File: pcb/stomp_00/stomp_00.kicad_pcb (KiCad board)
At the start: 2 copper layers, 54 x 106 mm, 48 parts, among them J1 9V_Power_Input, J10 AudioJack3, J11 AudioJack3, J2 Conn_01x09, J3 GuitarInput1, J4 Headphones, J5 GuitarOutput1, J6 Conn_01x09, J7 Conn_02x04_Counter_Clockwise, SW1 SW_DIP_x04, SW2 Footswitch, U14 6N138, U2 TL072, U4 XL1509-5.0, U5 AP7333-33SRG, U7 Teensy4.1, U9 SGTL5000XNAA3

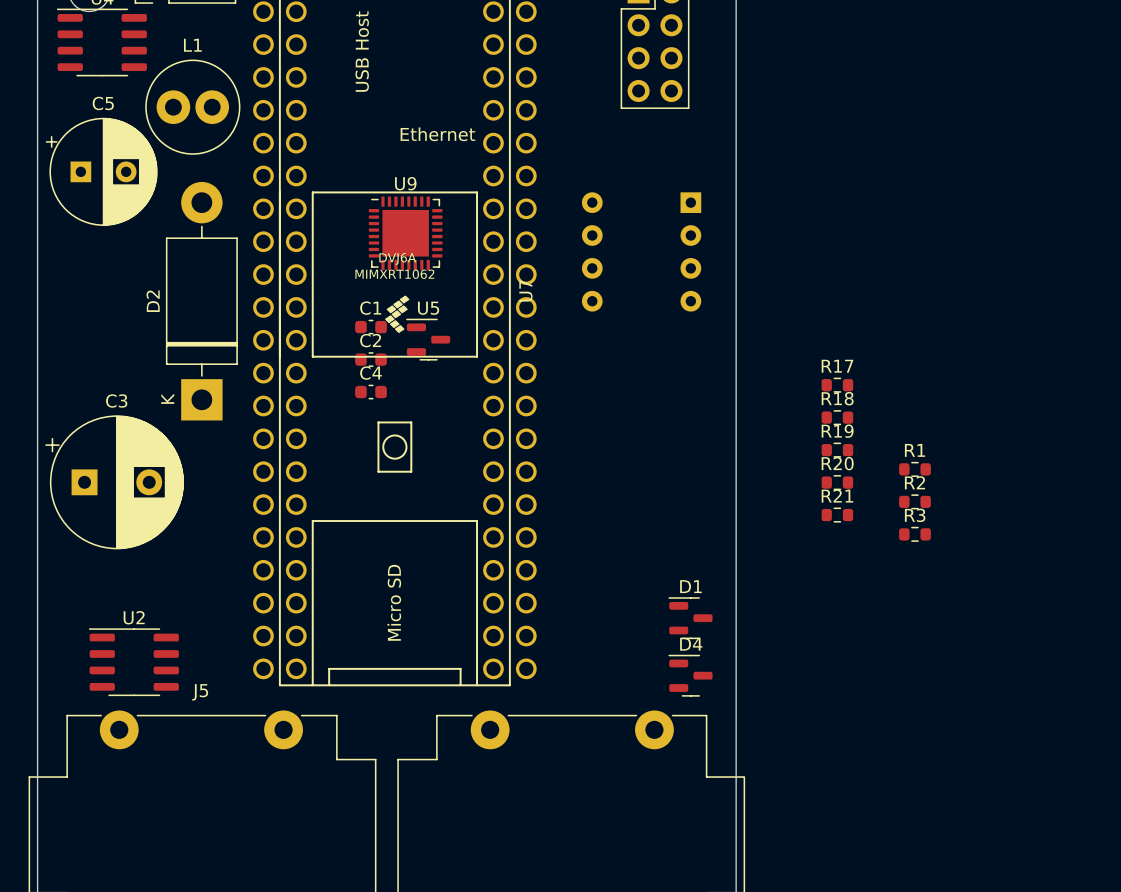
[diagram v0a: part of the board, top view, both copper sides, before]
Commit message: tweaking layout, issue with usb socket placement
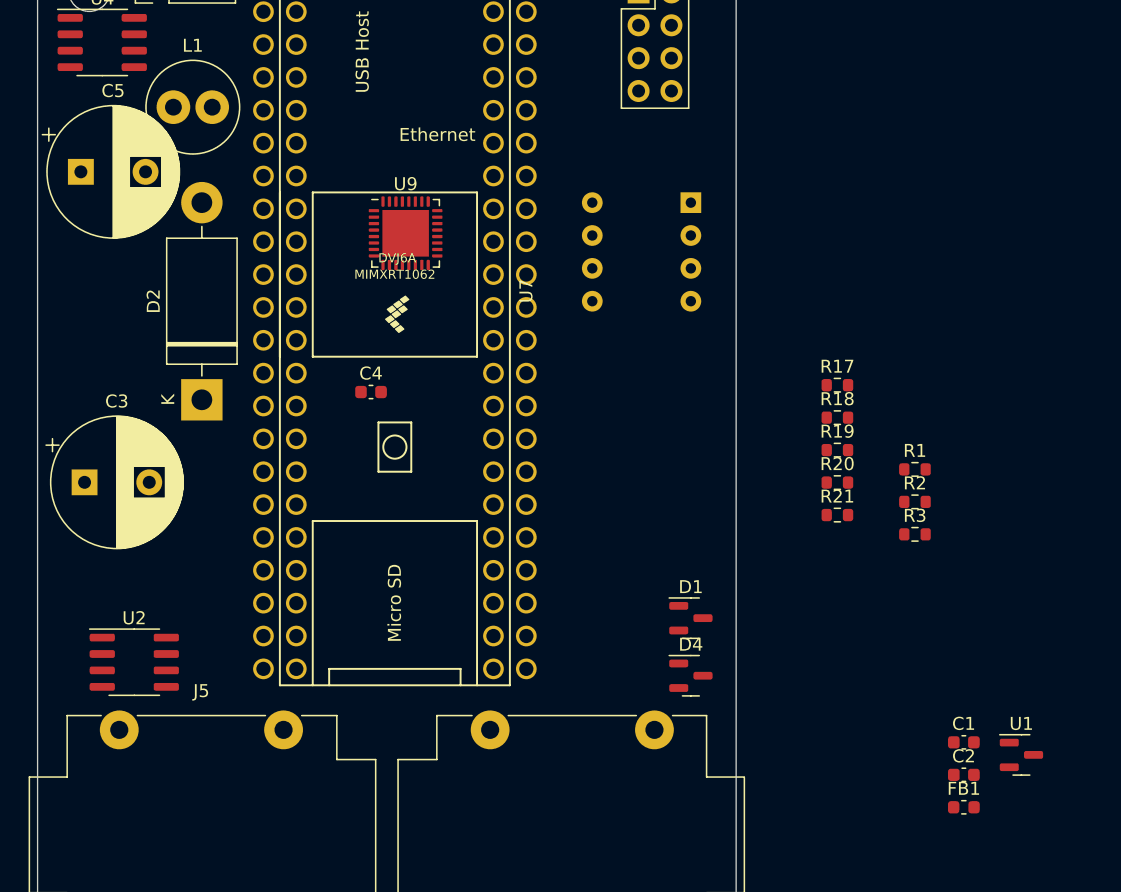
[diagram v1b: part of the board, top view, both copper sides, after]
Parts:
- removed U5: AP7333-33SRG, Package_TO_SOT_SMD:SOT-23
- added FB1: 600, Inductor_SMD:L_0603_1608Metric, F.Cu at (71.6, 71.1)
- added U1: AP7313-18SAG, Package_TO_SOT_SMD:SOT-23, F.Cu at (76.1, 67.1)
- C5: value 180uF 35V -> 470uF 25V; footprint Capacitor_THT:CP_Radial_D8.0mm_P3.50mm -> Capacitor_THT:CP_Radial_D10.0mm_P5.00mm
- J3, J5: footprint Connector_Audio:Jack_6.35mm_Neutrik_NMJ4HCD2_Horizontal -> stomp:Jack_6.35mm_Neutrik_NMJ4HCD2_Horizontal
- L1: value 68uH/2A -> 22uH/2A
- moved C2 56.0 mm to (71.6, 68.6)
- moved C1 56.0 mm to (71.6, 66.1)
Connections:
- net +3.3VDAC renamed +1V8
- C1 pad 1: +5V -> +3.3V
- U9 pad 5: +3.3V -> Net-(U9-VDDA)

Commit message: 9v power stuff
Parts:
- removed J1: 9V_Power_Input, Connector_PinHeader_2.54mm:PinHeader_1x03_P2.54mm_Vertical
- added J8: Barrel_Jack, Connector_PinHeader_2.54mm:PinHeader_1x02_P2.54mm_Vertical, F.Cu at (6.96, 2.00)
- moved C3 42.3 mm to (15.0, 5.25), turned to -90 degrees
- moved D2 39.0 mm to (23.5, 2.13), turned to -90 degrees
- moved SW1 37.8 mm to (23.6, 51.0)
- moved U2 28.0 mm to (35.5, 59.0)
- moved C4 26.4 mm to (16.5, 14.2)
- moved U9 18.8 mm to (40.5, 12.2)
- moved U4 12.9 mm to (16.5, 17.8)
- moved L1 12.6 mm to (20.8, 24.2)
- moved U7 10.0 mm to (37.6, 32.0)
- moved C5 7.40 mm to (9.87, 18.5), turned to 180 degrees

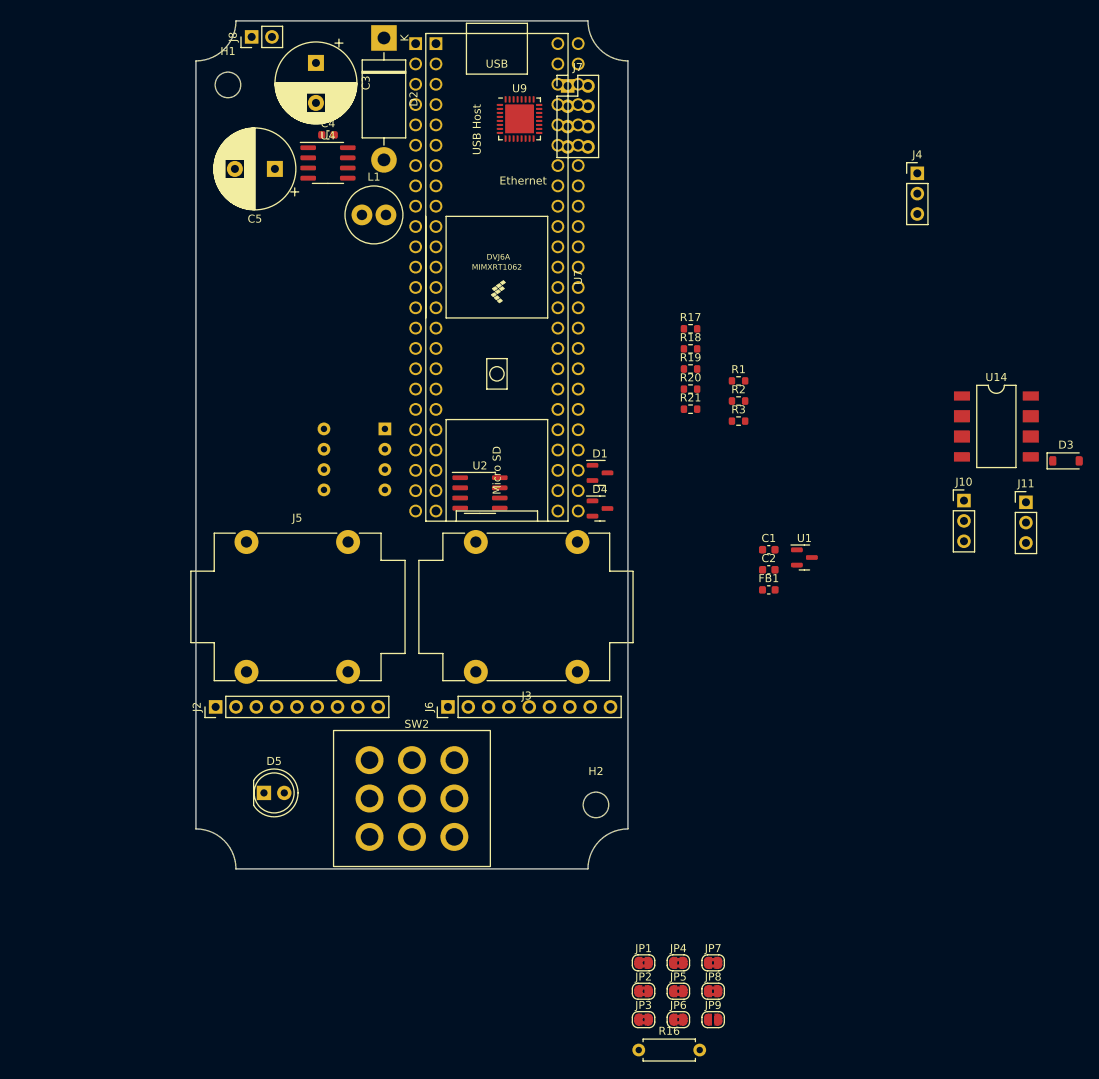
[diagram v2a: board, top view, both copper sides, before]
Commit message: changed voltage regulator
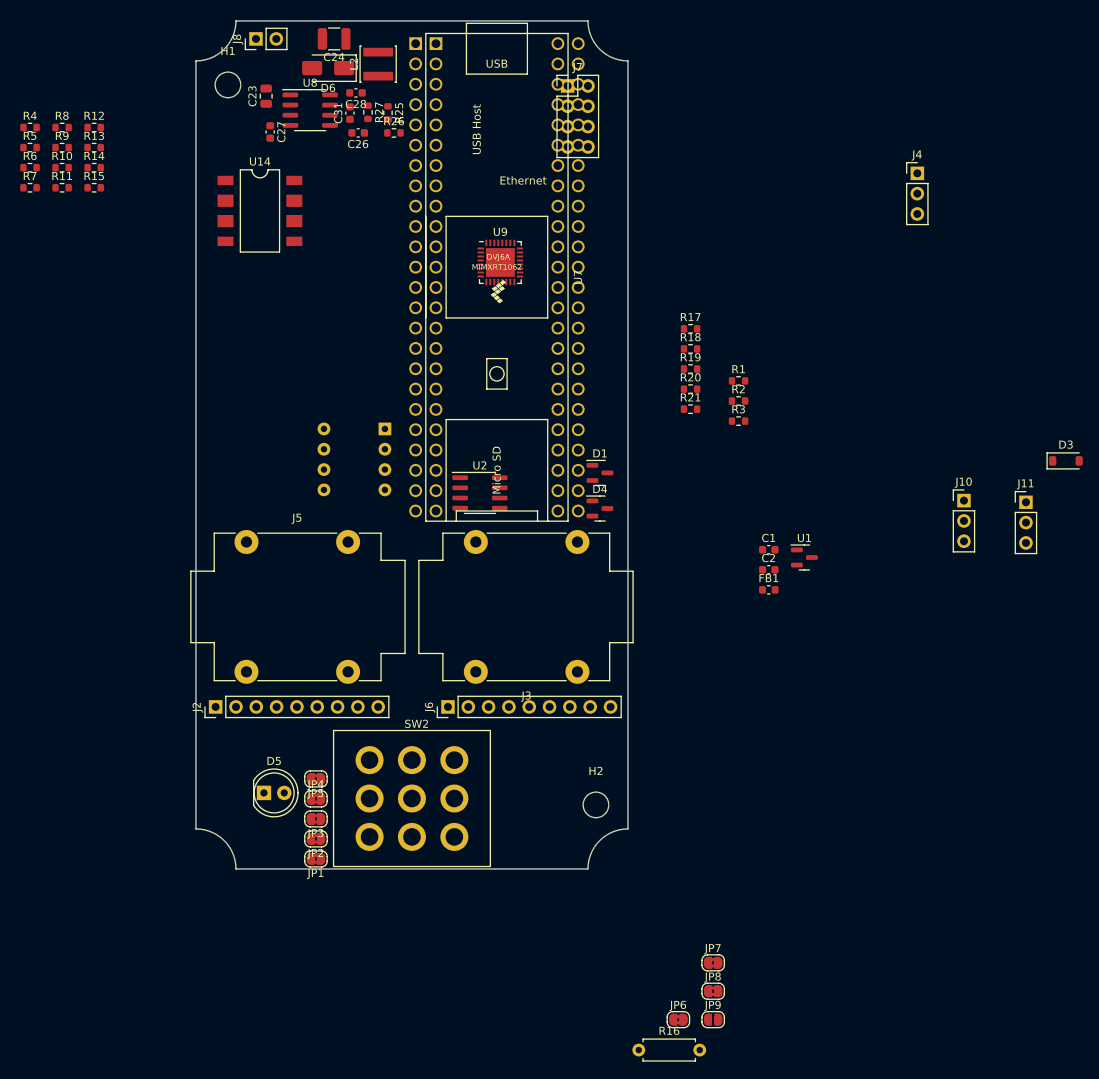
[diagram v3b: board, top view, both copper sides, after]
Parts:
- removed C3: 470uF 35V, Capacitor_THT:CP_Radial_D10.0mm_P5.00mm
- removed C4: 1uF, Capacitor_SMD:C_0603_1608Metric
- removed C5: 470uF 25V, Capacitor_THT:CP_Radial_D10.0mm_P5.00mm
- removed D2: 1N5820, Diode_THT:D_DO-201AD_P15.24mm_Horizontal
- removed L1: 22uH/2A, Inductor_THT:L_Radial_D7.0mm_P3.00mm
- removed U4: XL1509-5.0, Package_SO:SOIC-8_3.9x4.9mm_P1.27mm
- added C23: 22uF, Capacitor_SMD:C_0805_2012Metric, F.Cu at (8.78, 9.40)
- added C24: 47uF, Capacitor_SMD:C_1210_3225Metric, F.Cu at (17.3, 2.25)
- added C26: 1nF, Capacitor_SMD:C_0603_1608Metric, F.Cu at (20.3, 14.0)
- added C27: 10nF, Capacitor_SMD:C_0603_1608Metric, F.Cu at (9.28, 13.9)
- added C28: 100nF, Capacitor_SMD:C_0603_1608Metric, F.Cu at (20.0, 9.00)
- added C31: 10pF, Capacitor_SMD:C_0603_1608Metric, F.Cu at (19.2, 11.5)
- added D6: B340A, Diode_SMD:D_SMA, F.Cu at (16.5, 5.91)
- added L2: 6.8uH, Inductor_SMD:L_Changjiang_FNR4020S, F.Cu at (22.8, 5.41)
- added R10: 1M, Resistor_SMD:R_0603_1608Metric, F.Cu at (-16.7, 18.3)
- added R11: 2M, Resistor_SMD:R_0603_1608Metric, F.Cu at (-16.7, 20.9)
- added R12: 2M, Resistor_SMD:R_0603_1608Metric, F.Cu at (-12.7, 13.3)
- added R13: 10k, Resistor_SMD:R_0603_1608Metric, F.Cu at (-12.7, 15.8)
- added R14: 4.2k, Resistor_SMD:R_0603_1608Metric, F.Cu at (-12.7, 18.3)
- added R15: 1k, Resistor_SMD:R_0603_1608Metric, F.Cu at (-12.7, 20.9)
- added R25: 10k, Resistor_SMD:R_0603_1608Metric, F.Cu at (24.0, 11.5)
- added R26: 1.8k, Resistor_SMD:R_0603_1608Metric, F.Cu at (24.8, 14.0)
- added R27: 50k, Resistor_SMD:R_0603_1608Metric, F.Cu at (21.5, 11.4)
- added R4: 1M, Resistor_SMD:R_0603_1608Metric, F.Cu at (-20.7, 13.3)
- added R5: 10k, Resistor_SMD:R_0603_1608Metric, F.Cu at (-20.7, 15.8)
- added R6: 2M, Resistor_SMD:R_0603_1608Metric, F.Cu at (-20.7, 18.3)
- added R7: 2M, Resistor_SMD:R_0603_1608Metric, F.Cu at (-20.7, 20.9)
- added R8: 4.2k, Resistor_SMD:R_0603_1608Metric, F.Cu at (-16.7, 13.3)
- added R9: 1k, Resistor_SMD:R_0603_1608Metric, F.Cu at (-16.7, 15.8)
- added U8: TPS54331DR, Package_SO:SOIC-8_3.9x4.9mm_P1.27mm, F.Cu at (14.3, 11.2)
- moved U14 95.9 mm to (8.00, 23.8)
- moved JP5 52.5 mm to (15.0, 94.8), turned to 180 degrees
- moved JP4 49.7 mm to (15.0, 97.2)
- moved JP3 48.0 mm to (15.0, 99.8), turned to 180 degrees
- moved JP2 45.2 mm to (15.0, 102.2), turned to 180 degrees
- moved JP1 43.0 mm to (15.0, 104.8), turned to 180 degrees
- moved U9 18.1 mm to (38.0, 30.2)
- moved J8 0.60 mm to (7.50, 2.25)

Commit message: adding perfboard section
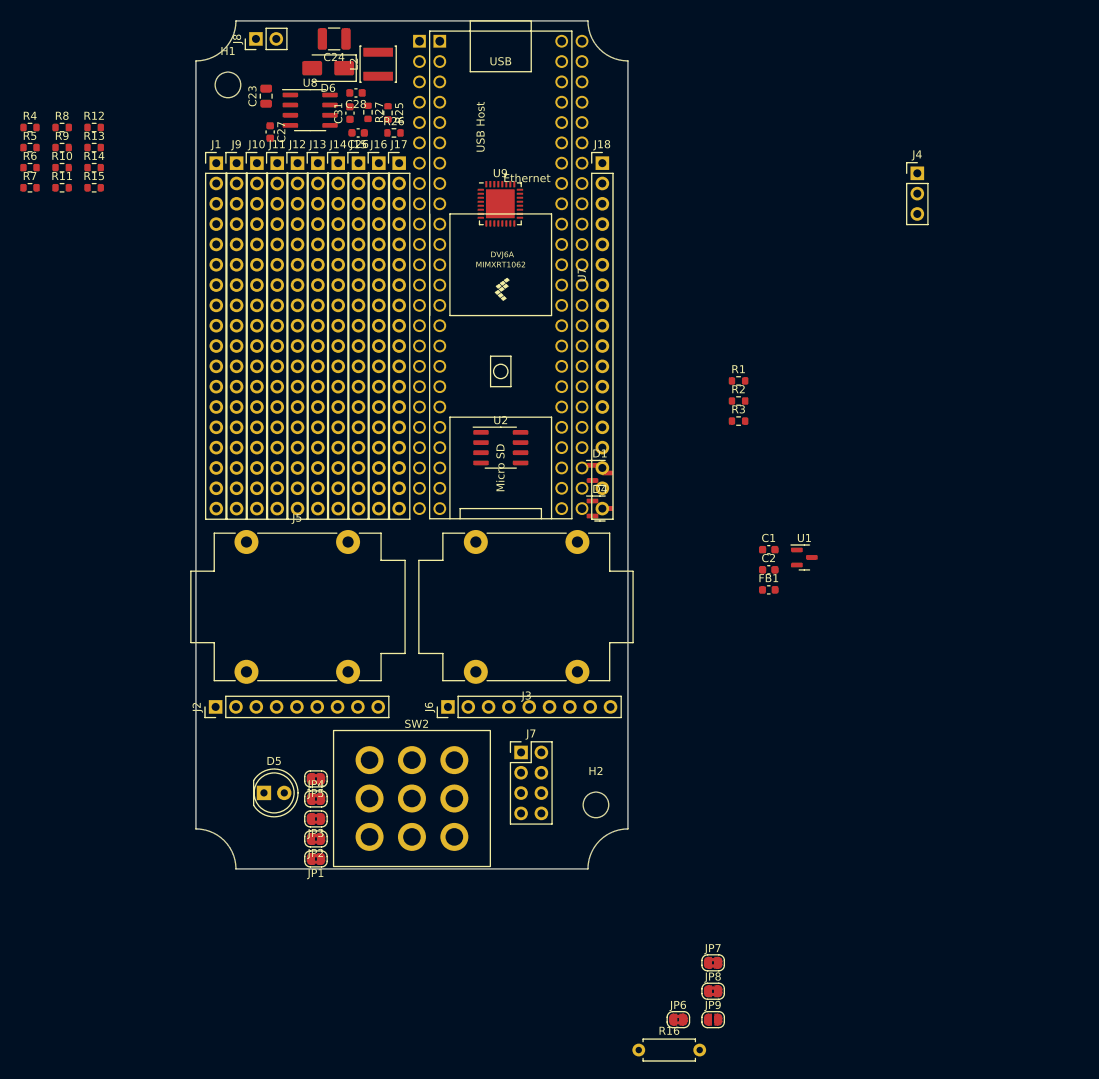
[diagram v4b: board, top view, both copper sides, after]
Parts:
- removed D3: 1N4148, Diode_SMD:D_SOD-123
- removed R17: 220R, Resistor_SMD:R_0603_1608Metric
- removed R18: 10k, Resistor_SMD:R_0603_1608Metric
- removed R19, R20: 47R, Resistor_SMD:R_0603_1608Metric
- removed R21: 470R, Resistor_SMD:R_0603_1608Metric
- removed SW1: SW_DIP_x04, Button_Switch_THT:SW_DIP_SPSTx04_Slide_9.78x12.34mm_W7.62mm_P2.54mm
- removed U14: 6N138, Package_DIP:PowerIntegrations_SMD-8
- added J1: Conn_01x18_Pin, Connector_PinHeader_2.54mm:PinHeader_1x18_P2.54mm_Vertical, F.Cu at (2.54, 17.8)
- added J12: Conn_01x18_Pin, Connector_PinHeader_2.54mm:PinHeader_1x18_P2.54mm_Vertical, F.Cu at (12.7, 17.8)
- added J13: Conn_01x18_Pin, Connector_PinHeader_2.54mm:PinHeader_1x18_P2.54mm_Vertical, F.Cu at (15.2, 17.8)
- added J14: Conn_01x18_Pin, Connector_PinHeader_2.54mm:PinHeader_1x18_P2.54mm_Vertical, F.Cu at (17.8, 17.8)
- added J15: Conn_01x18_Pin, Connector_PinHeader_2.54mm:PinHeader_1x18_P2.54mm_Vertical, F.Cu at (20.3, 17.8)
- added J16: Conn_01x18_Pin, Connector_PinHeader_2.54mm:PinHeader_1x18_P2.54mm_Vertical, F.Cu at (22.9, 17.8)
- added J17: Conn_01x18_Pin, Connector_PinHeader_2.54mm:PinHeader_1x18_P2.54mm_Vertical, F.Cu at (25.4, 17.8)
- added J18: Conn_01x18_Pin, Connector_PinHeader_2.54mm:PinHeader_1x18_P2.54mm_Vertical, F.Cu at (50.8, 17.8)
- added J9: Conn_01x18_Pin, Connector_PinHeader_2.54mm:PinHeader_1x18_P2.54mm_Vertical, F.Cu at (5.08, 17.8)
- J10, J11: value AudioJack3 -> Conn_01x18_Pin; footprint Connector_PinHeader_2.54mm:PinHeader_1x03_P2.54mm_Vertical -> Connector_PinHeader_2.54mm:PinHeader_1x18_P2.54mm_Vertical
- moved J11 102.7 mm to (10.2, 17.8)
- moved J10 97.9 mm to (7.62, 17.8)
- moved J7 83.5 mm to (40.6, 91.4)
- moved U9 7.34 mm to (38.0, 22.9)
- moved U2 6.23 mm to (38.1, 53.3)
- moved U7 0.57 mm to (38.1, 31.8)
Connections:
- J10 pad 1: (no net) -> unconnected-(J10-Pin_1-Pad1)
- J10 pad 2: (no net) -> unconnected-(J10-Pin_2-Pad2)
- J10 pad 3: (no net) -> unconnected-(J10-Pin_3-Pad3)
- J11 pad 1: (no net) -> unconnected-(J11-Pin_1-Pad1)
- J11 pad 2: (no net) -> unconnected-(J11-Pin_2-Pad2)
- J11 pad 3: (no net) -> unconnected-(J11-Pin_3-Pad3)

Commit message: tidying up footprints, layout, etc
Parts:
- removed J1: Conn_01x18_Pin, Connector_PinHeader_2.54mm:PinHeader_1x18_P2.54mm_Vertical
- removed J7: Conn_02x04_Counter_Clockwise, Connector_PinHeader_2.54mm:PinHeader_2x04_P2.54mm_Vertical
- J10, J11, J12, J13, J14, J15, J16, J17, J18, J9: footprint Connector_PinHeader_2.54mm:PinHeader_1x18_P2.54mm_Vertical -> stomp:PinHeader_1x18_P2.54mm_Vertical_perf
- J2: footprint Connector_PinHeader_2.54mm:PinHeader_1x09_P2.54mm_Vertical -> stomp:PinHeader_3x03_P2.54mm_Vertical_footswitch_breakout
- J6: value Conn_01x09 -> Conn_02x05_Counter_Clockwise; footprint Connector_PinHeader_2.54mm:PinHeader_1x09_P2.54mm_Vertical -> Connector_PinHeader_2.54mm:PinHeader_2x05_P2.54mm_Vertical
- JP1, JP2, JP3, JP4, JP5, JP6, JP7, JP8, JP9: moved to B.Cu
- moved JP6 71.3 mm to (10.0, 74.3), turned to 90 degrees
- moved JP8 67.6 mm to (16.0, 74.3), turned to 90 degrees
- moved JP7 67.5 mm to (13.0, 74.3), turned to 90 degrees
- moved R16 57.2 mm to (5.00, 101.6), turned to 90 degrees
- moved JP9 37.7 mm to (27.3, 129.5), turned to 180 degrees
- moved JP1 36.1 mm to (4.00, 70.3), turned to 90 degrees
- moved JP2 32.9 mm to (7.00, 70.3), turned to -90 degrees
- moved JP3 29.8 mm to (10.0, 70.3), turned to -90 degrees
- moved JP4 25.4 mm to (4.00, 74.3), turned to 90 degrees
- moved JP5 21.9 mm to (7.00, 74.3), turned to -90 degrees
- moved J6 18.6 mm to (44.0, 99.5), turned to 180 degrees
- moved J2 7.72 mm to (10.2, 86.4), turned to 0 degrees
- moved SW2 1.20 mm to (21.7, 91.2)
- moved D5 0.71 mm to (9.00, 96.0)
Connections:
- J3 pad T: Net-(J6-Pin_1) -> Net-(JP2-B)
- J6 pad 1: Net-(J6-Pin_1) -> unconnected-(J6-Pin_1-Pad1)
- J6 pad 9: Net-(D5-K) -> unconnected-(J6-Pin_9-Pad9)
- J9 pad 1: unconnected-(J9-Pin_1-Pad1) -> +3.3V
- J9 pad 16: unconnected-(J9-Pin_16-Pad16) -> GND
- J9 pad 17: unconnected-(J9-Pin_17-Pad17) -> GND
- J9 pad 18: unconnected-(J9-Pin_18-Pad18) -> GND
- J9 pad 2: unconnected-(J9-Pin_2-Pad2) -> +3.3V
- J9 pad 3: unconnected-(J9-Pin_3-Pad3) -> +3.3V
- JP2 pad 2: Net-(J6-Pin_1) -> Net-(JP2-B)
- JP9 pad 2: Net-(J6-Pin_1) -> Net-(JP2-B)
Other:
- board text added: "3.3V"
- board text added: "GND"
- board text added: "pedal in dac inL dac inR led neg gnd"
- board text added: "pedal out dac outL dac outR h/p L h/p R"

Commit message: tidying up dac connections
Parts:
- removed J4: Headphones, Connector_PinHeader_2.54mm:PinHeader_1x03_P2.54mm_Vertical
- removed U9: SGTL5000XNAA3, Package_DFN_QFN:QFN-32-1EP_5x5mm_P0.5mm_EP3.6x3.6mm
- added C10: 18p, Capacitor_SMD:C_0603_1608Metric, F.Cu at (64.1, 119.5)
- added C11: 1u, Capacitor_SMD:C_0603_1608Metric, F.Cu at (64.1, 122.0)
- added C12: 1n, Capacitor_SMD:C_0603_1608Metric, F.Cu at (64.1, 124.5)
- added C13: 0.1u, Capacitor_SMD:C_0603_1608Metric, F.Cu at (64.1, 127.0)
- added C14: 10u, Capacitor_SMD:C_0603_1608Metric, F.Cu at (68.2, 114.5)
- added C15: 18p, Capacitor_SMD:C_0603_1608Metric, F.Cu at (68.2, 117.0)
- added C16: 1n, Capacitor_SMD:C_0603_1608Metric, F.Cu at (68.2, 119.5)
- added C17: 1u, Capacitor_SMD:C_0603_1608Metric, F.Cu at (68.2, 122.0)
- added C18: 100n, Capacitor_SMD:C_0603_1608Metric, F.Cu at (68.2, 124.5)
- added C21: 1uF, Capacitor_SMD:C_0603_1608Metric, F.Cu at (78.2, 117.0)
- added C22: 1uF, Capacitor_SMD:C_0603_1608Metric, F.Cu at (78.2, 119.5)
- added C25: 0.15uF, Capacitor_SMD:C_0603_1608Metric, F.Cu at (78.2, 122.0)
- added C3: 0.1uF, Capacitor_SMD:C_0603_1608Metric, F.Cu at (74.2, 119.5)
- added C4: 0.1uF, Capacitor_SMD:C_0603_1608Metric, F.Cu at (74.2, 122.0)
- added C5: 2.2uF, Capacitor_SMD:C_0603_1608Metric, F.Cu at (74.2, 124.5)
- added C7: 10u, Capacitor_SMD:C_0603_1608Metric, F.Cu at (64.1, 114.5)
- added C8: 0.1u, Capacitor_SMD:C_0603_1608Metric, F.Cu at (64.1, 117.0)
- added C9: 0.1uF, Capacitor_SMD:C_0603_1608Metric, F.Cu at (78.2, 114.5)
- added J1: Headphones, Connector_PinHeader_2.54mm:PinHeader_1x03_P2.54mm_Vertical, F.Cu at (51.4, 87.0)
- added R17: 47k, Resistor_SMD:R_0603_1608Metric, F.Cu at (78.2, 124.5)
- added R18: 47k, Resistor_SMD:R_0603_1608Metric, F.Cu at (82.2, 114.5)
- added R19: 100R, Resistor_SMD:R_0603_1608Metric, F.Cu at (82.2, 117.0)
- added R20: 100R, Resistor_SMD:R_0603_1608Metric, F.Cu at (82.2, 119.5)
- added U3: SGTL5000XNLA3, Package_DFN_QFN:QFN-20-1EP_3x3mm_P0.4mm_EP1.65x1.65mm, F.Cu at (38.3, 27.5)
- C1, C2: value 1uF -> 2.2uF
- J2: value Conn_01x09 -> Footswitch_breakout
- moved U1 69.3 mm to (38.4, 8.89)
- moved FB1 62.5 mm to (38.1, 18.4), turned to 180 degrees
- moved C1 48.4 mm to (74.2, 114.5)
- moved C2 48.4 mm to (74.2, 117.0)
- moved JP9 46.6 mm to (43.2, 85.7)
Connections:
- C1 pad 1: +3.3V -> +1V8
- C2 pad 1: +1V8 -> +3.3V
